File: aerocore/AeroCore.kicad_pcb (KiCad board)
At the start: 2 copper layers, 60 x 60 mm, 61 parts, among them J1 USB_C_Receptacle_USB2.0_16P, J2 Conn_ARM_JTAG_SWD_10, J3 Conn_01x02_Pin, J4 Conn_01x06_Pin, Q1 DMG3418L, U1 RP2040, U2 AP2112K-3.3, U3 MCP73831-2-OT, U4 W25Q16JVUXIQ TR, U5 BMP388, U6 LIS3MDL, U7 ICM-20649, Y2 12MHz

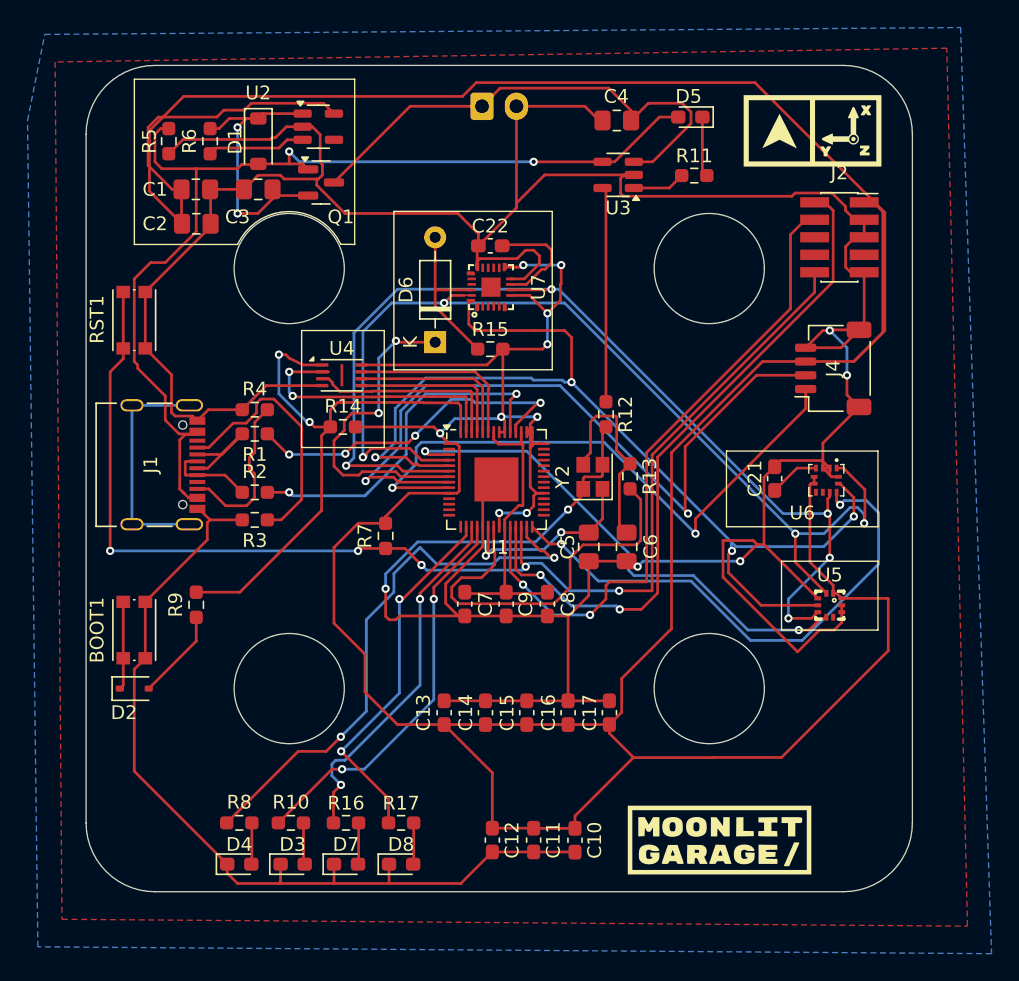
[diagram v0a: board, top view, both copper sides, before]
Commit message: update pcb schematic
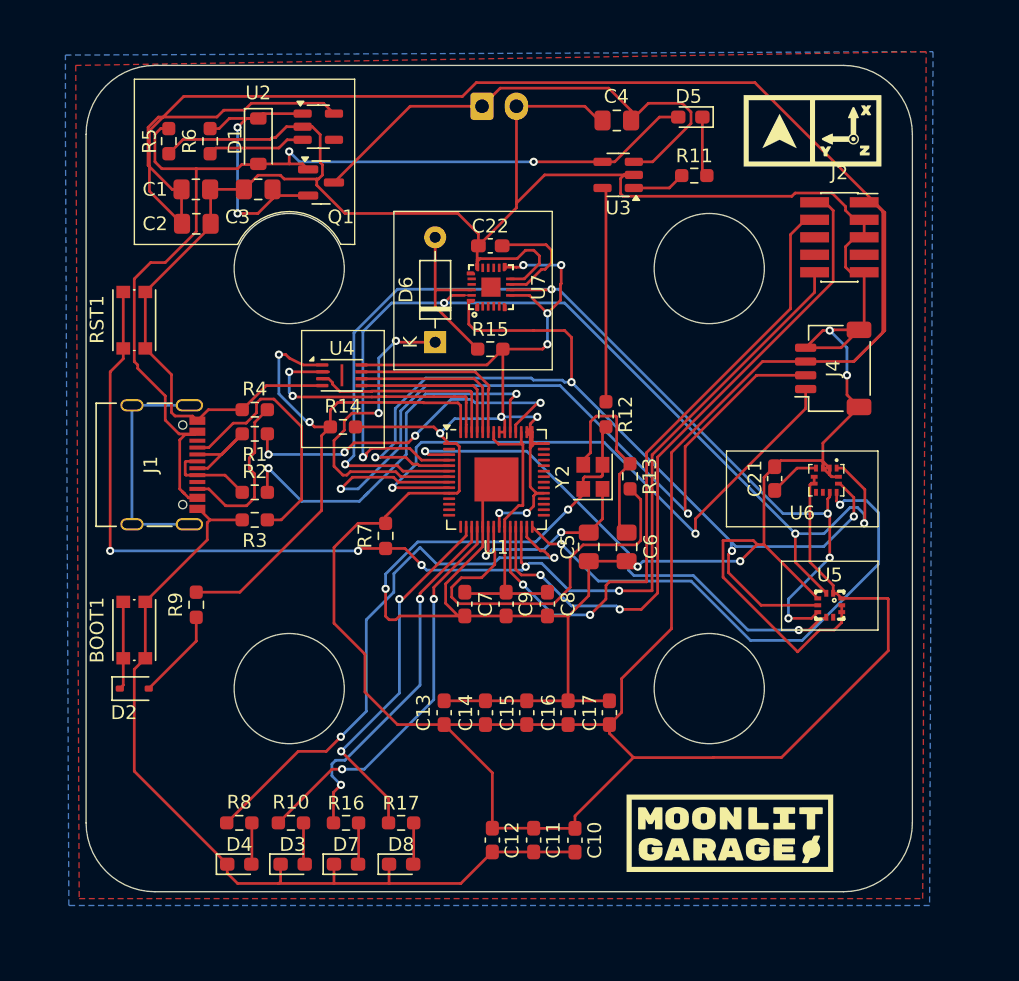
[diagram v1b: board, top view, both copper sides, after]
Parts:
- removed  : LOGO, LOGO
- added G***: LOGO, LOGO, F.Cu at (66.8, 185.8)
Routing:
- net /SDA: track 53.8 -> 57.9 mm
- net /D+: track 26.3 -> 29.1 mm
- net /D-: track 25.4 -> 26.3 mm
